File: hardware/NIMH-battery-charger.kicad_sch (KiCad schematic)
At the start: 28 parts, among them J1 Conn_01x03_Pin, J3 Conn_01x01_Pin, J4 Conn_01x01_Pin, J5 Conn_01x01_Pin, J6 Conn_01x01_Pin, J7 USB_C_Receptacle_PowerOnly_6P, U1 CH32V003f4u6

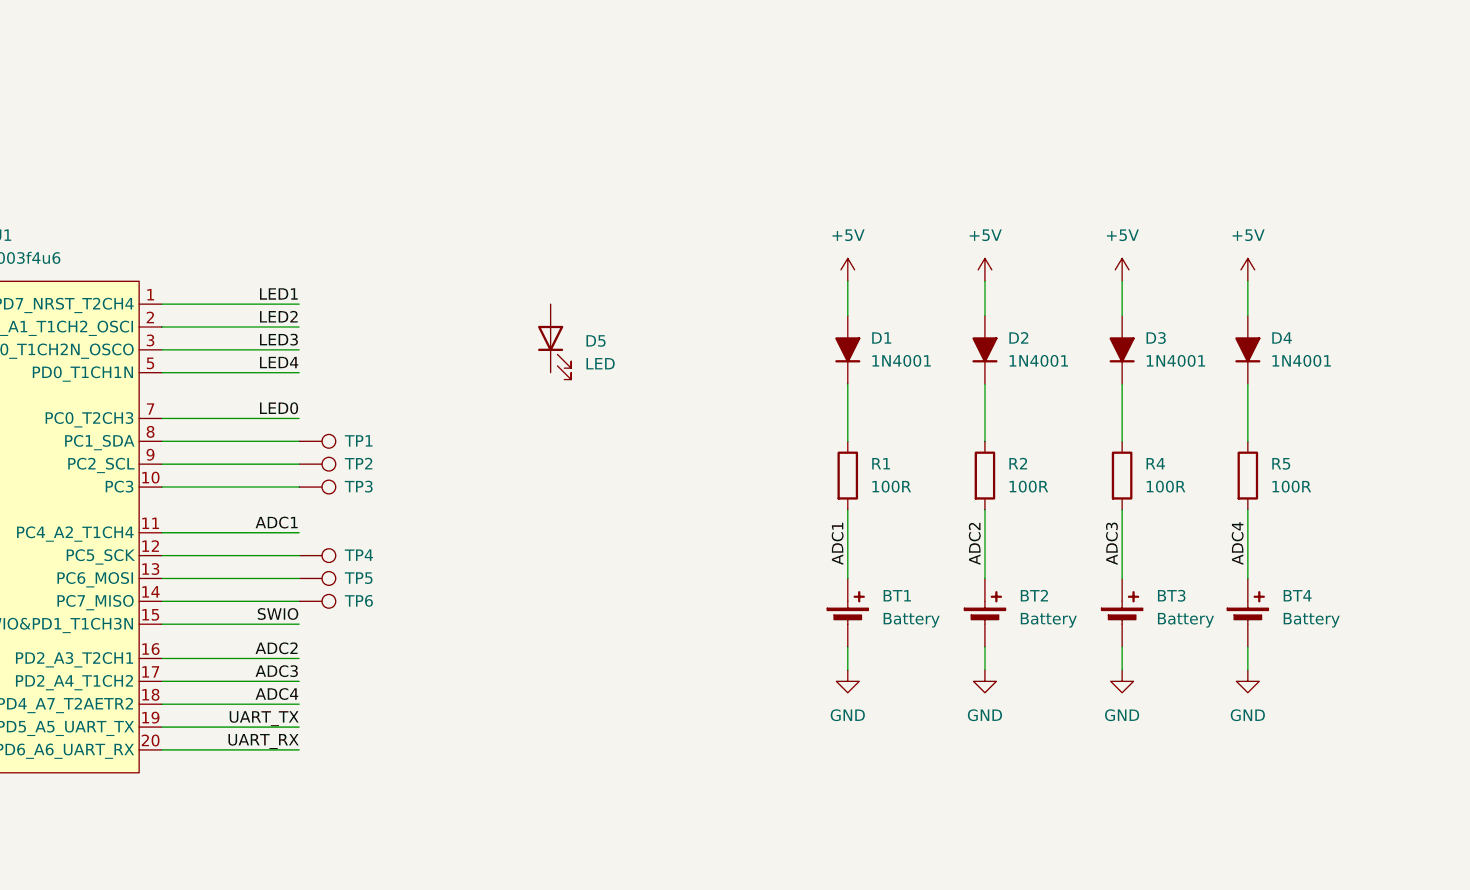
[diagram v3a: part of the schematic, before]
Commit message: Add leds
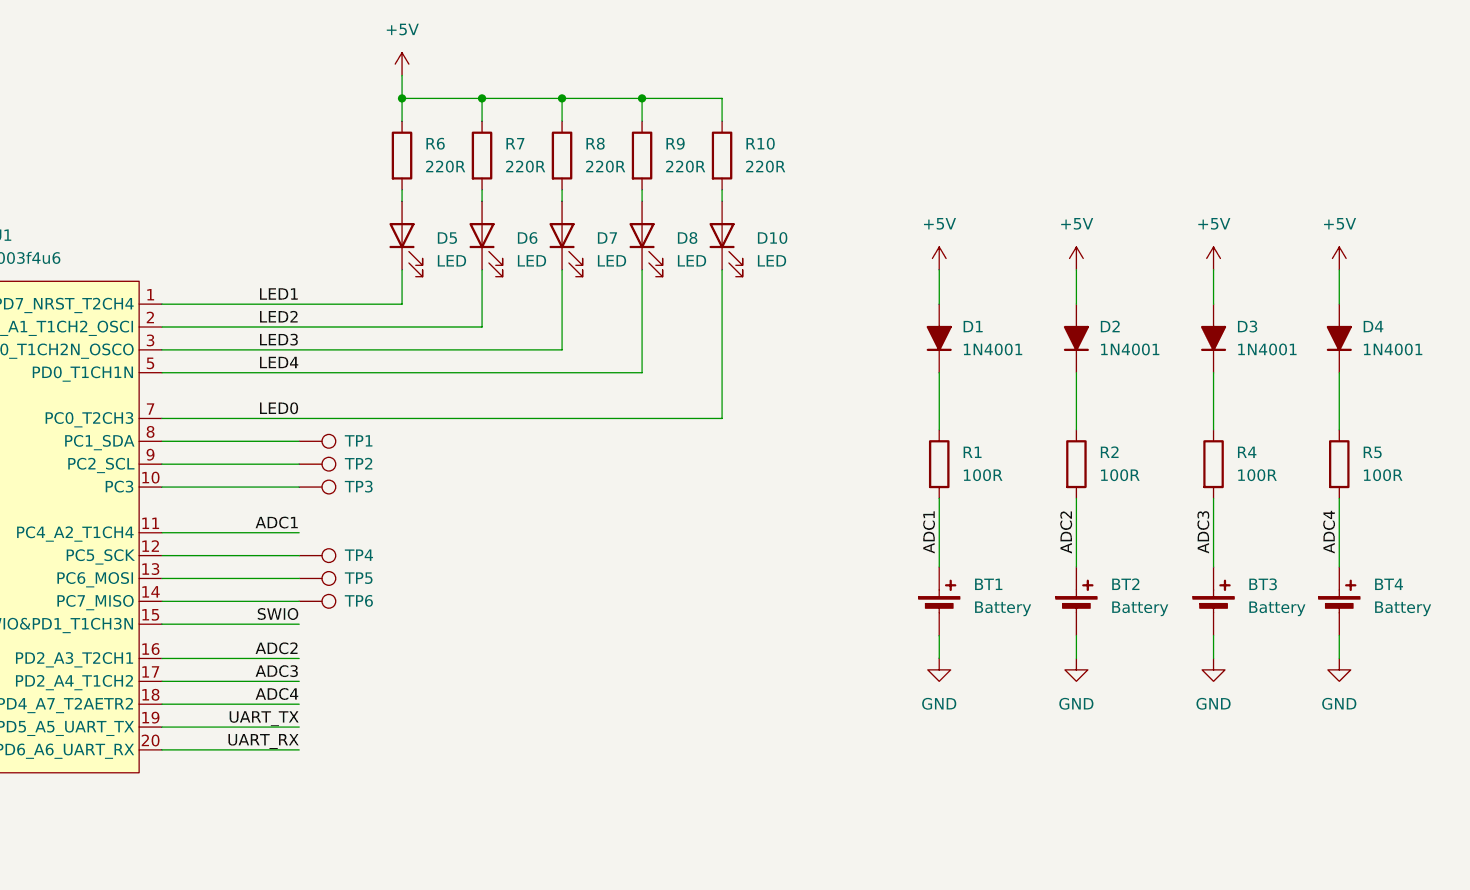
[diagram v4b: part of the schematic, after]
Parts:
- added D10, D6, D7, D8: LED, PCM_LED_SMD_AKL:LED_1206_3216Metric_ReverseMount_Hole1.8x2.4mm, symbol Device:LED
- added R10, R6, R7, R8, R9: 220R, PCM_Resistor_SMD_AKL:R_0805_2012Metric_Pad1.20x1.40mm_HandSolder, symbol Device:R
- D5: footprint (none) -> PCM_LED_SMD_AKL:LED_1206_3216Metric_ReverseMount_Hole1.8x2.4mm
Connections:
- net +5V: now also R10.1, R6.1, R7.1, R8.1, R9.1
- net LED0: now also D10.1 (K)
- net LED1: now also D5.1 (K)
- net LED2: now also D6.1 (K)
- net LED3: now also D7.1 (K)
- net LED4: now also D8.1 (K)
- net at D5.2 (A): now also R6.2
- new net: D10.2 (A), R10.2
- new net: D8.2 (A), R9.2
- new net: D6.2 (A), R7.2
- new net: D7.2 (A), R8.2
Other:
- moved on the sheet: BT1, BT2, BT3, BT4, D1, D2, D3, D4, D5, R1, R2, R4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

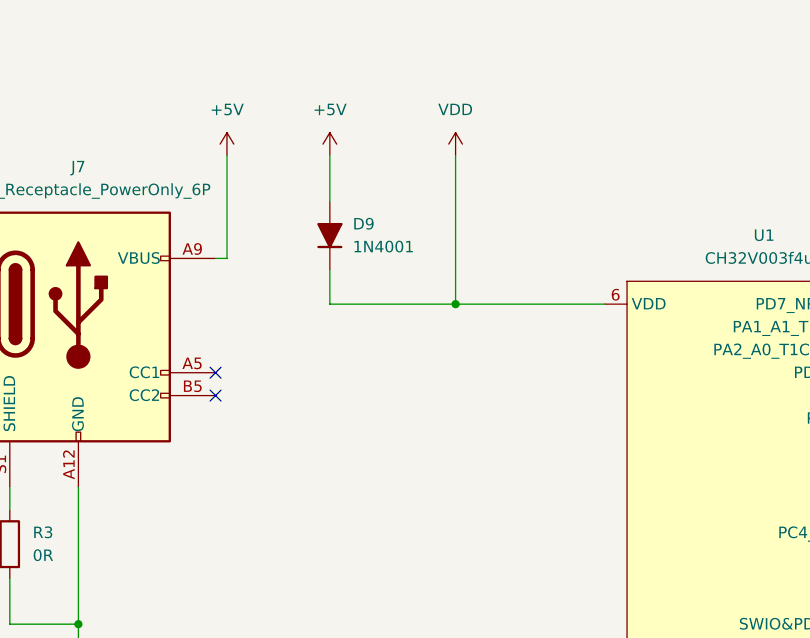
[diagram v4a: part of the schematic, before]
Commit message: Placed all components on board
Finalizing PCB
Add all components and place them for routing
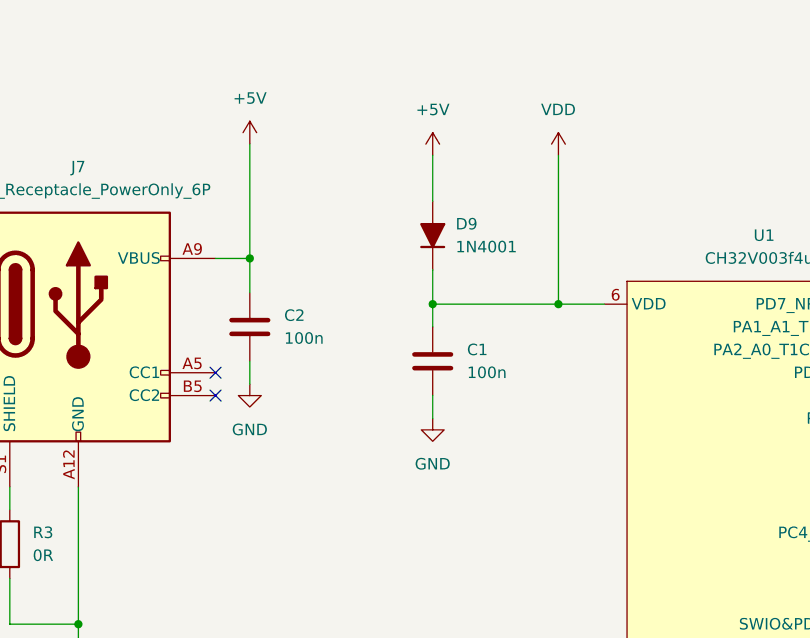
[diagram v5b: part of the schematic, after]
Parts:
- added C1, C2: 100n, PCM_Capacitor_SMD_AKL:C_0805_2012Metric_Pad1.18x1.45mm, symbol Device:C
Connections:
- net +5V: now also C2.1
- net GND: now also C1.2, C2.2
- net VDD: now also C1.1
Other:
- moved on the sheet: D9

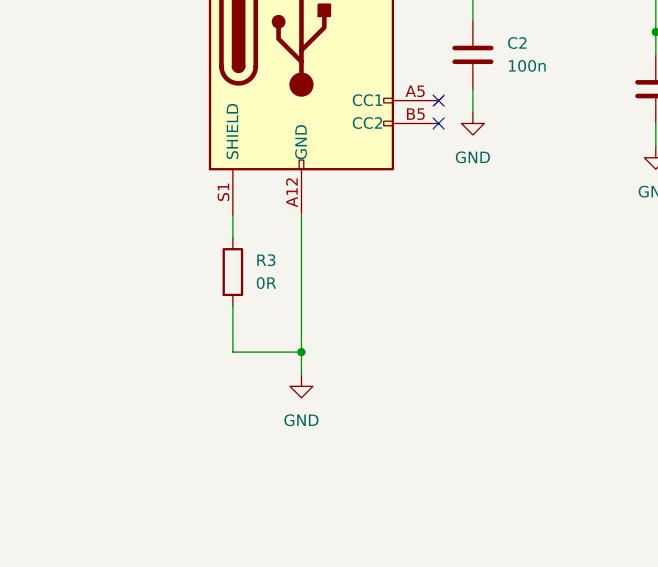
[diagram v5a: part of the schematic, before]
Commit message: Adding soild GND connection to some pins of USB connector
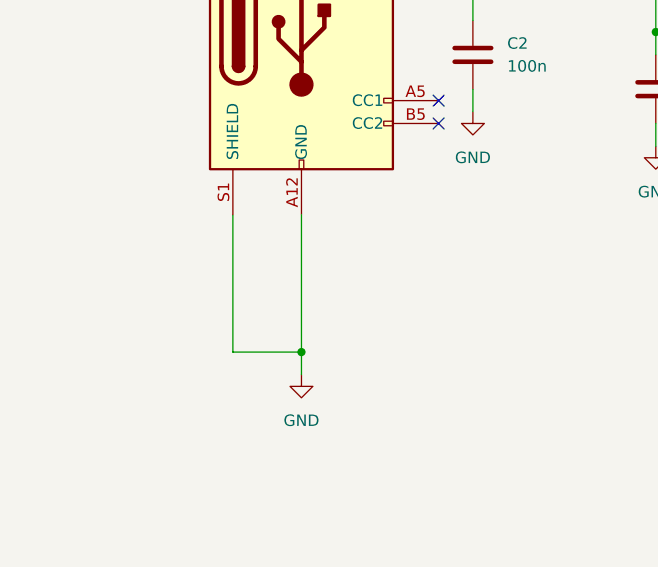
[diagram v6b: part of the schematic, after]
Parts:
- removed R3: 0R, PCM_Resistor_SMD_AKL:R_0603_1608Metric_Pad0.98x0.95mm_HandSolder, symbol Device:R
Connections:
- net GND: now also J7.S1 (SHIELD)
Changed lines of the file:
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@@
 	(wire
 		(pts
-			(xy 30.48 76.2) (xy 30.48 81.28)
-		)
-		(stroke
-			(width 0)
-			(type default)
-		)
-	)
-	(wire
-		(pts
 			(xy 132.08 60.96) (xy 147.32 60.96)
 		)
@@
 	(wire
 		(pts
-			(xy 30.48 66.04) (xy 30.48 68.58)
+			(xy 30.48 66.04) (xy 30.48 81.28)
 		)
 		(stroke
@@
 					(unit 1)
 				)
-			)
-		)
-	)
-	(symbol
-		(lib_id "Device:R")
-		(at 30.48 72.39 0)
-		(unit 1)
-		(exclude_from_sim no)
-		(in_bom yes)
-		(on_board yes)
-		(dnp no)
-		(fields_autoplaced yes)
-		(property "Reference" "R3"
-			(at 33.02 71.1199 0)
-			(effects
-				(font
-					(size 1.27 1.27)
-				)
-				(justify left)
-			)
-		)
-		(property "Value" "0R"
-			(at 33.02 73.6599 0)
-			(effects
-				(font
-					(size 1.27 1.27)
-				)
-				(justify left)
-			)
-		)
-		(property "Footprint" "PCM_Resistor_SMD_AKL:R_0603_1608Metric_Pad0.98x0.95mm_HandSolder"
-			(at 28.702 72.39 90)
-			(effects
-				(font
-					(size 1.27 1.27)
-				)
-				(hide yes)
-			)
-		)
-		(property "Datasheet" "~"
-			(at 30.48 72.39 0)
-			(effects
-				(font
-					(size 1.27 1.27)
-				)
-				(hide yes)
-			)
-		)
-		(property "Description" "Resistor"
-			(at 30.48 72.39 0)
-			(effects
-				(font
-					(size 1.27 1.27)
-				)
-				(hide yes)
-			)
-		)
-		(pin "2"
-		)
-		(pin "1"
-		)
-		(instances
-			(project "NIMH-battery-charger"
-				(path "/0d2dca8c-c927-4122-be5b-6109da7ea2cf"
-					(reference "R3")
-					(unit 1)
-				)

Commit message: Completed routing board
Created gergers for JLCPCB
Added mounting holes
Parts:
- added H1, H2, H3, H4: MountingHole, MountingHole:MountingHole_3.2mm_M3_ISO14580_Pad_TopOnly, symbol Mechanical:MountingHole
- added TP7, TP8: TestPoint, TestPoint:TestPoint_Pad_D1.5mm, symbol Connector:TestPoint
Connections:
- net ADC1: now also U1.17 (PD2_A4_T1CH2); no longer U1.11 (PC4_A2_T1CH4)
- net ADC2: now also U1.18 (PD4_A7_T2AETR2); no longer U1.16 (PD2_A3_T2CH1)
- net ADC3: now also U1.11 (PC4_A2_T1CH4); no longer U1.17 (PD2_A4_T1CH2)
- net ADC4: now also U1.16 (PD2_A3_T2CH1); no longer U1.18 (PD4_A7_T2AETR2)
- net UART_RX: now also TP8.1
- net UART_TX: now also TP7.1
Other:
- moved on the sheet: J1
